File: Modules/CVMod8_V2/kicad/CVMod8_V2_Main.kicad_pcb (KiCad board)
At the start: 2 copper layers, 100.8 x 85 mm, 68 parts, among them U1 TL074, U10 79L05, U2 TL074, U3 TL074, U4 TL074, U5 TL074, U6 TL074, U7 TL074, U8 TL074, U9 78L05

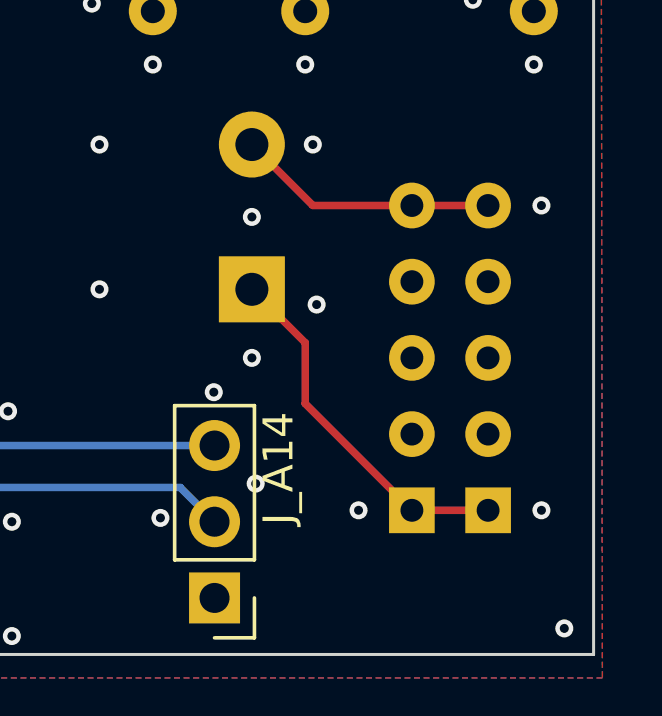
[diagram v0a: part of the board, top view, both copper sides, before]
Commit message: Add Interactive BOMs, resave all PCBs, move VU to THT.
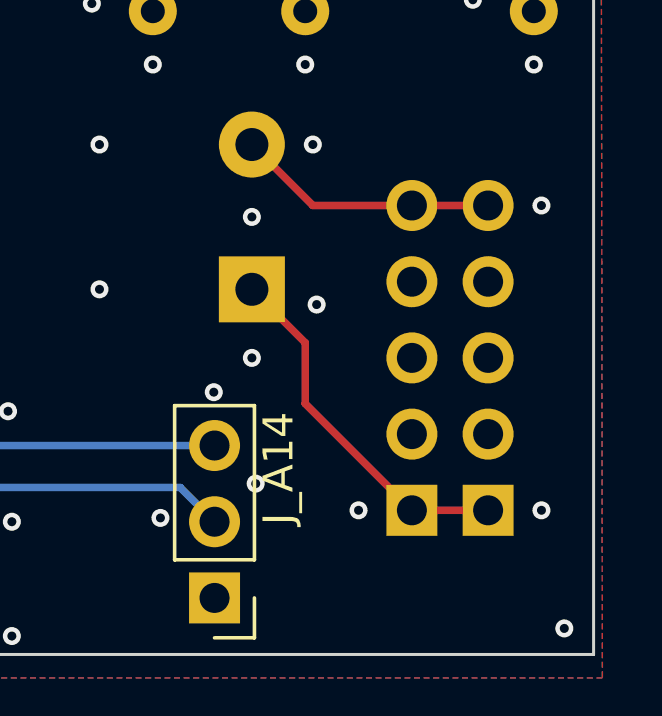
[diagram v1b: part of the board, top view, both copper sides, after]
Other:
- board text added: "CVMod8 V2 v2.1"
- board text removed: "CVMod8 V2 v2.0"
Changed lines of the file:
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@@
 	)
 	(paper "A4")
+	(title_block
+		(rev "v2.1")
+	)
 	(layers
 		(0 "F.Cu" jumper)
@@
 		(attr through_hole)
 		(fp_line
-			(start 3.24 -7.62)
-			(end -0.7 -7.62)
+			(start 3.24 -6.858)
+			(end -0.7 -6.858)
 			(stroke
 				(width 0.5)
@@
 		(pad "1" thru_hole circle
 			(at 0 5.08 180)
-			(size 1.524 1.524)
-			(drill 0.762)
+			(size 1.7 1.7)
+			(drill 1)
 			(layers "*.Cu" "*.Mask")
 			(remove_unused_layers no)
@@
 		(pad "1" thru_hole circle
 			(at 2.54 5.08 180)
-			(size 1.524 1.524)
-			(drill 0.762)
+			(size 1.7 1.7)
+			(drill 1)
 			(layers "*.Cu" "*.Mask")
 			(remove_unused_layers no)
@@
 		(pad "2" thru_hole circle
 			(at 0 -2.54 180)
-			(size 1.524 1.524)
-			(drill 0.762)
+			(size 1.7 1.7)
+			(drill 1)
 			(layers "*.Cu" "*.Mask")
 			(remove_unused_layers no)
@@
 		(pad "2" thru_hole circle
 			(at 0 0 180)
-			(size 1.524 1.524)
-			(drill 0.762)
+			(size 1.7 1.7)
+			(drill 1)
 			(layers "*.Cu" "*.Mask")
 			(remove_unused_layers no)
@@
 		(pad "2" thru_hole circle
 			(at 0 2.54 180)
-			(size 1.524 1.524)
-			(drill 0.762)
+			(size 1.7 1.7)
+			(drill 1)
 			(layers "*.Cu" "*.Mask")
 			(remove_unused_layers no)
@@
 		(pad "2" thru_hole circle
 			(at 2.54 -2.54 180)
-			(size 1.524 1.524)
-			(drill 0.762)
+			(size 1.7 1.7)
+			(drill 1)
 			(layers "*.Cu" "*.Mask")
 			(remove_unused_layers no)
@@
 		(pad "2" thru_hole circle
 			(at 2.54 0 180)
-			(size 1.524 1.524)
-			(drill 0.762)
+			(size 1.7 1.7)
+			(drill 1)
 			(layers "*.Cu" "*.Mask")
 			(remove_unused_layers no)
@@
 		(pad "2" thru_hole circle
 			(at 2.54 2.54 180)
-			(size 1.524 1.524)
-			(drill 0.762)
+			(size 1.7 1.7)
+			(drill 1)
 			(layers "*.Cu" "*.Mask")
 			(remove_unused_layers no)
@@
 		(pad "3" thru_hole rect
 			(at 0 -5.08 180)
-			(size 1.524 1.524)
-			(drill 0.762)
+			(size 1.7 1.7)
+			(drill 1)
 			(layers "*.Cu" "*.Mask")
 			(remove_unused_layers no)
@@
 		(pad "3" thru_hole rect
 			(at 2.54 -5.08 180)
-			(size 1.524 1.524)
-			(drill 0.762)
+			(size 1.7 1.7)
+			(drill 1)
 			(layers "*.Cu" "*.Mask")
 			(remove_unused_layers no)
@@
 		(layer "Edge.Cuts")
 	)
-	(gr_text "CVMod8 V2 v2.0"
+	(gr_text "CVMod8 V2 v2.1"
 		(at 62.484 139.446 0)
 		(layer "B.SilkS")

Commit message: Release SMD CVMod8 V2.
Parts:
- removed J_A1, J_A2, J_A3, J_A4, J_A5, J_A6, J_A7, J_A8: Conn_01x06_Male, Connector_PinHeader_2.54mm:PinHeader_1x06_P2.54mm_Vertical
- removed J_A11, J_A12, J_A13, J_A14: Conn_01x03_Male, Connector_PinHeader_2.54mm:PinHeader_1x03_P2.54mm_Vertical
- removed the REF** at (116.1, 148.1)
- removed the REF** at (65.7, 148.1)
- removed the REF** at (125.1, 73.0)
- removed the REF** at (49.5, 73.0)
- removed RN1, RN10, RN11, RN12, RN13, RN14, RN15, RN16, RN2, RN3, RN4, RN5, RN6, RN7, RN8, RN9: 100k, Resistor_THT:R_Array_SIP8
- added J_IN1: PJ301M-12, Eurorack:PJ301M-12 Offset, F.Cu at (46.8, 59.4)
- added J_IN2: PJ301M-12, Eurorack:PJ301M-12 Offset, F.Cu at (59.4, 59.4)
- added J_IN3: PJ301M-12, Eurorack:PJ301M-12 Offset, F.Cu at (72.0, 59.4)
- added J_IN4: PJ301M-12, Eurorack:PJ301M-12 Offset, F.Cu at (84.6, 59.4)
- added J_IN5: PJ301M-12, Eurorack:PJ301M-12 Offset, F.Cu at (97.2, 59.4)
- added J_IN6: PJ301M-12, Eurorack:PJ301M-12 Offset, F.Cu at (109.8, 59.4)
- added J_IN7: PJ301M-12, Eurorack:PJ301M-12 Offset, F.Cu at (122.4, 59.4)
- added J_IN8: PJ301M-12, Eurorack:PJ301M-12 Offset, F.Cu at (135.0, 59.4)
- added J_OUT1: PJ301M-12, Eurorack:PJ301M-12 Offset, F.Cu at (46.8, 48.2)
- added J_OUT2: PJ301M-12, Eurorack:PJ301M-12 Offset, F.Cu at (59.4, 48.2)
- added J_OUT3: PJ301M-12, Eurorack:PJ301M-12 Offset, F.Cu at (72.0, 48.2)
- added J_OUT4: PJ301M-12, Eurorack:PJ301M-12 Offset, F.Cu at (84.6, 48.2)
- added J_OUT5: PJ301M-12, Eurorack:PJ301M-12 Offset, F.Cu at (97.2, 48.2)
- added J_OUT6: PJ301M-12, Eurorack:PJ301M-12 Offset, F.Cu at (109.8, 48.2)
- added J_OUT7: PJ301M-12, Eurorack:PJ301M-12 Offset, F.Cu at (122.4, 48.2)
- added J_OUT8: PJ301M-12, Eurorack:PJ301M-12 Offset, F.Cu at (135.0, 48.2)
- added LD1: LED (Bi), LED_THT:LED_D3.0mm_FlatTop, F.Cu at (46.8, 77.6)
- added LD2: LED (Bi), LED_THT:LED_D3.0mm_FlatTop, F.Cu at (59.4, 77.6)
- added LD3: LED (Bi), LED_THT:LED_D3.0mm_FlatTop, F.Cu at (72.0, 77.6)
- added LD4: LED (Bi), LED_THT:LED_D3.0mm_FlatTop, F.Cu at (84.6, 77.6)
- added LD5: LED (Bi), LED_THT:LED_D3.0mm_FlatTop, F.Cu at (97.2, 77.6)
- added LD6: LED (Bi), LED_THT:LED_D3.0mm_FlatTop, F.Cu at (109.8, 77.6)
- added LD7: LED (Bi), LED_THT:LED_D3.0mm_FlatTop, F.Cu at (122.4, 77.6)
- added LD8: LED (Bi), LED_THT:LED_D3.0mm_FlatTop, F.Cu at (135.0, 77.6)
- added P_ATN1: B100k, Eurorack:Potentiometer Song Huei 9mm Trimmer, F.Cu at (46.8, 86.9)
- added P_ATN2: B100k, Eurorack:Potentiometer Song Huei 9mm Trimmer, F.Cu at (59.4, 86.9)
- added P_ATN3: B100k, Eurorack:Potentiometer Song Huei 9mm Trimmer, F.Cu at (72.0, 86.9)
- added P_ATN4: B100k, Eurorack:Potentiometer Song Huei 9mm Trimmer, F.Cu at (84.6, 86.9)
- added P_ATN5: B100k, Eurorack:Potentiometer Song Huei 9mm Trimmer, F.Cu at (97.2, 86.9)
- added P_ATN6: B100k, Eurorack:Potentiometer Song Huei 9mm Trimmer, F.Cu at (109.8, 86.9)
- added P_ATN7: B100k, Eurorack:Potentiometer Song Huei 9mm Trimmer, F.Cu at (122.4, 86.9)
- added P_ATN8: B100k, Eurorack:Potentiometer Song Huei 9mm Trimmer, F.Cu at (135.0, 86.9)
- added P_OFS1: B100k, Potentiometer_THT:Potentiometer_Bourns_PTA3043_Single_Slide, F.Cu at (48.6, 99.1)
- added P_OFS2: B100k, Potentiometer_THT:Potentiometer_Bourns_PTA3043_Single_Slide, F.Cu at (61.2, 99.1)
- added P_OFS3: B100k, Potentiometer_THT:Potentiometer_Bourns_PTA3043_Single_Slide, F.Cu at (73.8, 99.1)
- added P_OFS4: B100k, Potentiometer_THT:Potentiometer_Bourns_PTA3043_Single_Slide, F.Cu at (86.3, 99.1)
- added P_OFS5: B100k, Potentiometer_THT:Potentiometer_Bourns_PTA3043_Single_Slide, F.Cu at (99.0, 99.1)
- added P_OFS6: B100k, Potentiometer_THT:Potentiometer_Bourns_PTA3043_Single_Slide, F.Cu at (111.6, 99.1)
- added P_OFS7: B100k, Potentiometer_THT:Potentiometer_Bourns_PTA3043_Single_Slide, F.Cu at (124.2, 99.1)
- added P_OFS8: B100k, Potentiometer_THT:Potentiometer_Bourns_PTA3043_Single_Slide, F.Cu at (136.7, 99.1)
- added R10: 1k, Resistor_SMD:R_0603_1608Metric_Pad0.98x0.95mm_HandSolder, B.Cu at (59.3, 84.8)
- added R11: 1k, Resistor_SMD:R_0603_1608Metric_Pad0.98x0.95mm_HandSolder, B.Cu at (72.0, 84.8)
- added R12: 1k, Resistor_SMD:R_0603_1608Metric_Pad0.98x0.95mm_HandSolder, B.Cu at (84.6, 84.8)
- added R13: 1k, Resistor_SMD:R_0603_1608Metric_Pad0.98x0.95mm_HandSolder, B.Cu at (97.3, 84.8)
- added R14: 1k, Resistor_SMD:R_0603_1608Metric_Pad0.98x0.95mm_HandSolder, B.Cu at (109.7, 84.8)
- added R15: 1k, Resistor_SMD:R_0603_1608Metric_Pad0.98x0.95mm_HandSolder, B.Cu at (122.4, 84.8)
- added R16: 1k, Resistor_SMD:R_0603_1608Metric_Pad0.98x0.95mm_HandSolder, B.Cu at (135.0, 84.8)
- added R17: 100k, Resistor_SMD:R_0603_1608Metric_Pad0.98x0.95mm_HandSolder, B.Cu at (50.8, 120.2)
- added R18: 100k, Resistor_SMD:R_0603_1608Metric_Pad0.98x0.95mm_HandSolder, B.Cu at (47.0, 120.2)
- added R19: 100k, Resistor_SMD:R_0603_1608Metric_Pad0.98x0.95mm_HandSolder, B.Cu at (43.2, 120.2)
- added R20: 100k, Resistor_SMD:R_0603_1608Metric_Pad0.98x0.95mm_HandSolder, B.Cu at (50.8, 123.6)
- added R21: 100k, Resistor_SMD:R_0603_1608Metric_Pad0.98x0.95mm_HandSolder, B.Cu at (47.0, 123.6)
- added R22: 100k, Resistor_SMD:R_0603_1608Metric_Pad0.98x0.95mm_HandSolder, B.Cu at (43.2, 123.6)
- added R23: 100k, Resistor_SMD:R_0603_1608Metric_Pad0.98x0.95mm_HandSolder, B.Cu at (47.0, 127.0)
- added R24: 100k, Resistor_SMD:R_0603_1608Metric_Pad0.98x0.95mm_HandSolder, B.Cu at (63.3, 120.2)
- added R25: 100k, Resistor_SMD:R_0603_1608Metric_Pad0.98x0.95mm_HandSolder, B.Cu at (59.5, 120.2)
- added R26: 100k, Resistor_SMD:R_0603_1608Metric_Pad0.98x0.95mm_HandSolder, B.Cu at (55.7, 120.2)
- added R27: 100k, Resistor_SMD:R_0603_1608Metric_Pad0.98x0.95mm_HandSolder, B.Cu at (63.3, 123.6)
- added R28: 100k, Resistor_SMD:R_0603_1608Metric_Pad0.98x0.95mm_HandSolder, B.Cu at (59.5, 123.6)
- added R29: 100k, Resistor_SMD:R_0603_1608Metric_Pad0.98x0.95mm_HandSolder, B.Cu at (55.7, 123.6)
- added R30: 100k, Resistor_SMD:R_0603_1608Metric_Pad0.98x0.95mm_HandSolder, B.Cu at (63.3, 127.0)
- added R31: 100k, Resistor_SMD:R_0603_1608Metric_Pad0.98x0.95mm_HandSolder, B.Cu at (59.5, 127.0)
- added R32: 100k, Resistor_SMD:R_0603_1608Metric_Pad0.98x0.95mm_HandSolder, B.Cu at (75.9, 120.2)
- added R33: 100k, Resistor_SMD:R_0603_1608Metric_Pad0.98x0.95mm_HandSolder, B.Cu at (72.1, 120.2)
- added R34: 100k, Resistor_SMD:R_0603_1608Metric_Pad0.98x0.95mm_HandSolder, B.Cu at (68.3, 120.2)
- added R35: 100k, Resistor_SMD:R_0603_1608Metric_Pad0.98x0.95mm_HandSolder, B.Cu at (75.9, 123.6)
- added R36: 100k, Resistor_SMD:R_0603_1608Metric_Pad0.98x0.95mm_HandSolder, B.Cu at (72.1, 123.6)
- added R37: 100k, Resistor_SMD:R_0603_1608Metric_Pad0.98x0.95mm_HandSolder, B.Cu at (68.3, 123.6)
- added R38: 100k, Resistor_SMD:R_0603_1608Metric_Pad0.98x0.95mm_HandSolder, B.Cu at (75.9, 127.0)
- added R39: 100k, Resistor_SMD:R_0603_1608Metric_Pad0.98x0.95mm_HandSolder, B.Cu at (72.1, 127.0)
- added R40: 100k, Resistor_SMD:R_0603_1608Metric_Pad0.98x0.95mm_HandSolder, B.Cu at (88.5, 120.2)
- added R41: 100k, Resistor_SMD:R_0603_1608Metric_Pad0.98x0.95mm_HandSolder, B.Cu at (84.7, 120.2)
- added R42: 100k, Resistor_SMD:R_0603_1608Metric_Pad0.98x0.95mm_HandSolder, B.Cu at (80.9, 120.2)
- added R43: 100k, Resistor_SMD:R_0603_1608Metric_Pad0.98x0.95mm_HandSolder, B.Cu at (88.5, 123.6)
- added R44: 100k, Resistor_SMD:R_0603_1608Metric_Pad0.98x0.95mm_HandSolder, B.Cu at (84.7, 123.6)
- added R45: 100k, Resistor_SMD:R_0603_1608Metric_Pad0.98x0.95mm_HandSolder, B.Cu at (80.9, 123.6)
- added R46: 100k, Resistor_SMD:R_0603_1608Metric_Pad0.98x0.95mm_HandSolder, B.Cu at (88.5, 127.0)
- added R47: 100k, Resistor_SMD:R_0603_1608Metric_Pad0.98x0.95mm_HandSolder, B.Cu at (84.7, 127.0)
- added R48: 100k, Resistor_SMD:R_0603_1608Metric_Pad0.98x0.95mm_HandSolder, B.Cu at (101.1, 120.2)
- added R49: 100k, Resistor_SMD:R_0603_1608Metric_Pad0.98x0.95mm_HandSolder, B.Cu at (97.3, 120.2)
- added R50: 100k, Resistor_SMD:R_0603_1608Metric_Pad0.98x0.95mm_HandSolder, B.Cu at (93.5, 120.2)
- added R51: 100k, Resistor_SMD:R_0603_1608Metric_Pad0.98x0.95mm_HandSolder, B.Cu at (101.1, 123.6)
- added R52: 100k, Resistor_SMD:R_0603_1608Metric_Pad0.98x0.95mm_HandSolder, B.Cu at (97.3, 123.6)
- added R53: 100k, Resistor_SMD:R_0603_1608Metric_Pad0.98x0.95mm_HandSolder, B.Cu at (93.5, 123.6)
- added R54: 100k, Resistor_SMD:R_0603_1608Metric_Pad0.98x0.95mm_HandSolder, B.Cu at (101.1, 127.0)
- added R55: 100k, Resistor_SMD:R_0603_1608Metric_Pad0.98x0.95mm_HandSolder, B.Cu at (97.3, 127.0)
- added R56: 100k, Resistor_SMD:R_0603_1608Metric_Pad0.98x0.95mm_HandSolder, B.Cu at (113.7, 120.2)
- added R57: 100k, Resistor_SMD:R_0603_1608Metric_Pad0.98x0.95mm_HandSolder, B.Cu at (109.9, 120.2)
- added R58: 100k, Resistor_SMD:R_0603_1608Metric_Pad0.98x0.95mm_HandSolder, B.Cu at (106.0, 120.2)
- added R59: 100k, Resistor_SMD:R_0603_1608Metric_Pad0.98x0.95mm_HandSolder, B.Cu at (113.7, 123.6)
- added R60: 100k, Resistor_SMD:R_0603_1608Metric_Pad0.98x0.95mm_HandSolder, B.Cu at (109.9, 123.6)
- added R61: 100k, Resistor_SMD:R_0603_1608Metric_Pad0.98x0.95mm_HandSolder, B.Cu at (106.0, 123.6)
- added R62: 100k, Resistor_SMD:R_0603_1608Metric_Pad0.98x0.95mm_HandSolder, B.Cu at (113.7, 127.0)
- added R63: 100k, Resistor_SMD:R_0603_1608Metric_Pad0.98x0.95mm_HandSolder, B.Cu at (109.9, 127.0)
- added R64: 100k, Resistor_SMD:R_0603_1608Metric_Pad0.98x0.95mm_HandSolder, B.Cu at (126.3, 120.2)
- added R65: 100k, Resistor_SMD:R_0603_1608Metric_Pad0.98x0.95mm_HandSolder, B.Cu at (122.5, 120.2)
- added R66: 100k, Resistor_SMD:R_0603_1608Metric_Pad0.98x0.95mm_HandSolder, B.Cu at (118.7, 120.2)
- added R67: 100k, Resistor_SMD:R_0603_1608Metric_Pad0.98x0.95mm_HandSolder, B.Cu at (126.3, 123.6)
- added R68: 100k, Resistor_SMD:R_0603_1608Metric_Pad0.98x0.95mm_HandSolder, B.Cu at (122.5, 123.6)
- added R69: 100k, Resistor_SMD:R_0603_1608Metric_Pad0.98x0.95mm_HandSolder, B.Cu at (118.7, 123.6)
- added R70: 100k, Resistor_SMD:R_0603_1608Metric_Pad0.98x0.95mm_HandSolder, B.Cu at (126.3, 127.0)
- added R71: 100k, Resistor_SMD:R_0603_1608Metric_Pad0.98x0.95mm_HandSolder, B.Cu at (122.5, 127.0)
- added R72: 100k, Resistor_SMD:R_0603_1608Metric_Pad0.98x0.95mm_HandSolder, B.Cu at (138.9, 120.2)
- added R73: 100k, Resistor_SMD:R_0603_1608Metric_Pad0.98x0.95mm_HandSolder, B.Cu at (135.1, 120.2)
- added R74: 100k, Resistor_SMD:R_0603_1608Metric_Pad0.98x0.95mm_HandSolder, B.Cu at (131.3, 120.2)
- added R75: 100k, Resistor_SMD:R_0603_1608Metric_Pad0.98x0.95mm_HandSolder, B.Cu at (138.9, 123.6)
- added R76: 100k, Resistor_SMD:R_0603_1608Metric_Pad0.98x0.95mm_HandSolder, B.Cu at (135.1, 123.6)
- added R77: 100k, Resistor_SMD:R_0603_1608Metric_Pad0.98x0.95mm_HandSolder, B.Cu at (131.3, 123.6)
- added R78: 100k, Resistor_SMD:R_0603_1608Metric_Pad0.98x0.95mm_HandSolder, B.Cu at (138.9, 127.0)
- added R79: 100k, Resistor_SMD:R_0603_1608Metric_Pad0.98x0.95mm_HandSolder, B.Cu at (135.1, 127.0)
- added R9: 1k, Resistor_SMD:R_0603_1608Metric_Pad0.98x0.95mm_HandSolder, B.Cu at (46.9, 84.8)
- added REF**: M2 Screw Hole, Eurorack:M2 Screw Hole, F.Cu at (128.7, 96.0)
- added REF**: M2 Screw Hole, Eurorack:M2 Screw Hole, F.Cu at (103.5, 96.0)
- added REF**: M2 Screw Hole, Eurorack:M2 Screw Hole, F.Cu at (53.1, 96.0)
- added REF**: M2 Screw Hole, Eurorack:M2 Screw Hole, F.Cu at (78.3, 96.0)
- added SW_FWD1: SW_SPDT, Eurorack:SPDT, F.Cu at (50.3, 68.5)
- added SW_FWD2: SW_SPDT, Eurorack:SPDT, F.Cu at (62.9, 68.5)
- added SW_FWD3: SW_SPDT, Eurorack:SPDT, F.Cu at (75.5, 68.5)
- added SW_FWD4: SW_SPDT, Eurorack:SPDT, F.Cu at (88.1, 68.5)
- added SW_FWD5: SW_SPDT, Eurorack:SPDT, F.Cu at (100.7, 68.5)
- added SW_FWD6: SW_SPDT, Eurorack:SPDT, F.Cu at (113.3, 68.5)
- added SW_FWD7: SW_SPDT, Eurorack:SPDT, F.Cu at (125.9, 68.5)
- added SW_POL1: SW_SPDT, Eurorack:SPDT, F.Cu at (46.8, 147.6)
- added SW_POL2: SW_SPDT, Eurorack:SPDT, F.Cu at (59.4, 147.6)
- added SW_POL3: SW_SPDT, Eurorack:SPDT, F.Cu at (72.0, 147.6)
- added SW_POL4: SW_SPDT, Eurorack:SPDT, F.Cu at (84.6, 147.6)
- added SW_POL5: SW_SPDT, Eurorack:SPDT, F.Cu at (97.2, 147.6)
- added SW_POL6: SW_SPDT, Eurorack:SPDT, F.Cu at (109.8, 147.6)
- added SW_POL7: SW_SPDT, Eurorack:SPDT, F.Cu at (122.4, 147.6)
- added SW_POL8: SW_SPDT, Eurorack:SPDT, F.Cu at (135.0, 147.6)
- C1, C2: footprint Capacitor_THT:CP_Radial_D6.3mm_P2.50mm -> Capacitor_SMD:CP_Elec_6.3x5.3
- C10, C11, C12, C13, C14, C3, C4, C5, C6, C7, C8, C9: footprint Capacitor_THT:C_Disc_D7.0mm_W2.5mm_P5.00mm -> Capacitor_SMD:C_0603_1608Metric_Pad1.08x0.95mm_HandSolder
- D1, D2: value 1N4001 -> FM4001; footprint Diode_THT:D_DO-41_SOD81_P10.16mm_Horizontal -> Eurorack:D_SOD-123F_AH
- R1, R2, R3, R4, R5, R6, R7, R8: footprint Resistor_THT:R_Axial_DIN0207_L6.3mm_D2.5mm_P10.16mm_Horizontal -> Resistor_SMD:R_0603_1608Metric_Pad0.98x0.95mm_HandSolder
- U1, U2, U3, U4, U5, U6, U7, U8: footprint Package_DIP:DIP-14_W7.62mm_Socket_LongPads -> Eurorack:SO-14_3.9x8.65mm_P1.27mm_AH
- U10, U9: footprint Package_TO_SOT_THT:TO-92_Inline_Wide -> Package_TO_SOT_SMD:SOT-89-3_Handsoldering
- moved PWR1 72.7 mm to (104.7, 75.7)
- moved D1 66.1 mm to (97.8, 71.0)
- moved C10 65.7 mm to (78.5, 115.6), turned to 90 degrees
- moved D2 65.3 mm to (98.0, 81.2)
- moved C1 64.0 mm to (90.7, 73.3), turned to 180 degrees
- moved C2 61.6 mm to (90.4, 80.4), turned to 0 degrees
- moved C11 52.3 mm to (103.6, 108.5), turned to 90 degrees
- moved C4 51.1 mm to (92.6, 98.0), turned to -90 degrees
- moved U9 45.1 mm to (91.0, 92.4), turned to 90 degrees
- moved C8 45.0 mm to (53.2, 115.6), turned to 90 degrees
- moved C3 41.6 mm to (89.4, 98.0), turned to -90 degrees
- moved C9 40.4 mm to (78.5, 108.5), turned to 90 degrees
- moved R1 36.3 mm to (46.8, 46.4)
- moved R6 36.3 mm to (109.8, 46.4)
- moved R2 36.3 mm to (59.4, 46.4)
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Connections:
- C10 pad 1: GND -> -12V
- C10 pad 2: +12V -> GND
- C11 pad 1: -12V -> GND
- C11 pad 2: GND -> +12V
- C13 pad 1: -12V -> GND
- C13 pad 2: GND -> +12V
- C4 pad 1: GND -> +5V
- C4 pad 2: -12V -> GND
- C5 pad 1: +5V -> GND
- C5 pad 2: GND -> -12V
- C8 pad 1: GND -> -12V
- C8 pad 2: +12V -> GND
- R1 pad 1: Net-(RN1C-R3.1) -> /OUT1
- R1 pad 2: /LED1 -> Net-(J_OUT1-PadSIG)
- R2 pad 1: Net-(RN3C-R3.1) -> /OUT2
- R2 pad 2: /LED2 -> Net-(J_OUT2-PadSIG)
- R3 pad 1: Net-(RN5C-R3.1) -> /OUT3
- R3 pad 2: /LED3 -> Net-(J_OUT3-PadSIG)
- R4 pad 1: Net-(RN7C-R3.1) -> /OUT4
- R4 pad 2: /LED4 -> Net-(J_OUT4-PadSIG)
- R5 pad 1: Net-(RN10D-R4.2) -> /OUT5
- R5 pad 2: /LED5 -> Net-(J_OUT5-PadSIG)
- R6 pad 1: Net-(RN11C-R3.1) -> /OUT6
- R6 pad 2: /LED6 -> Net-(J_OUT6-PadSIG)
- R7 pad 1: Net-(RN13C-R3.1) -> /OUT7
- R7 pad 2: /LED7 -> Net-(J_OUT7-PadSIG)
- R8 pad 1: Net-(RN15C-R3.1) -> /OUT8
- R8 pad 2: /LED8 -> Net-(J_OUT8-PadSIG)
- U1 pad 8: Net-(RN1C-R3.1) -> Net-(R22-Pad1)
- U2 pad 8: Net-(RN3C-R3.1) -> Net-(R10-Pad1)
- U3 pad 8: Net-(RN5C-R3.1) -> Net-(R11-Pad1)
- U4 pad 8: Net-(RN7C-R3.1) -> Net-(R12-Pad1)
- U5 pad 8: Net-(RN10D-R4.2) -> Net-(R13-Pad1)
- U6 pad 8: Net-(RN11C-R3.1) -> Net-(R14-Pad1)
- U7 pad 8: Net-(RN13C-R3.1) -> Net-(R15-Pad1)
- U8 pad 8: Net-(RN15C-R3.1) -> Net-(R16-Pad1)
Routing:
- net /FWD5: track 0.00 -> 66.3 mm, vias 0 -> 7
- net /FWD3: track 0.00 -> 64.7 mm, vias 0 -> 7
- net /FWD1: track 0.00 -> 64.6 mm, vias 0 -> 7
- net /FWD6: track 0.00 -> 64.6 mm, vias 0 -> 7
- net /FWD2: track 0.00 -> 64.6 mm, vias 0 -> 7
- net /FWD7: track 0.00 -> 64.6 mm, vias 0 -> 5
- net /FWD4: track 0.00 -> 64.6 mm, vias 0 -> 7
- net Net-(J_IN6-PadSIG): track 0.00 -> 60.4 mm, vias 0 -> 4
- net Net-(J_IN7-PadSIG): track 0.00 -> 60.4 mm, vias 0 -> 4
- net Net-(J_IN3-PadSIG): track 0.00 -> 60.4 mm, vias 0 -> 4
- net Net-(J_IN5-PadSIG): track 0.00 -> 60.4 mm, vias 0 -> 4
- net Net-(J_IN4-PadSIG): track 0.00 -> 60.4 mm, vias 0 -> 4
- net Net-(J_IN2-PadSIG): track 0.00 -> 60.4 mm, vias 0 -> 4
- net Net-(J_IN1-PadSIG): track 0.00 -> 60.3 mm, vias 0 -> 2
- net Net-(J_IN8-PadSIG): track 0.00 -> 60.1 mm, vias 0 -> 4
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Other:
- board size 100.8 x 85 mm -> 100.8 x 108.6 mm
- board text added: "CVMod8 V2 v2.2"
- board text removed: "CVMod8 V2 v2.1"
